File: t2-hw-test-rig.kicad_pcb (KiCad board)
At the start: 2 copper layers, 86.4 x 94 mm, 158 parts, among them J101 CONN_01X02, J102 BARREL_JACK, J103 CONN_01X02, J201 MICROUSB-TH, J202 CONN_01X02, J203 MICROUSB-TH, J204 USB_A_TH, J301 CONN_02x05, 0.05", Q101 pMOS, Q401 CJ2302, Q402 CJ2302, Q403 CJ2302, Q404 CJ2302, SW301 Switch_DPST, SW302 Switch_DPST, U101 MAX6102, U102 XC6206P332MR-G, U301 ATSAMD21J18A-MUT, U302 AAT4610, U303 AAT4610, U401 MAX9919FASA+, U402 MAX9919FASA+, U403 MAX9919FASA+, U404 MAX9919FASA+, U405 MAX9919FASA+, U501 TSV324IDT, U502 TSV324IDT, U503 TSV324IDT, X301 FC-135

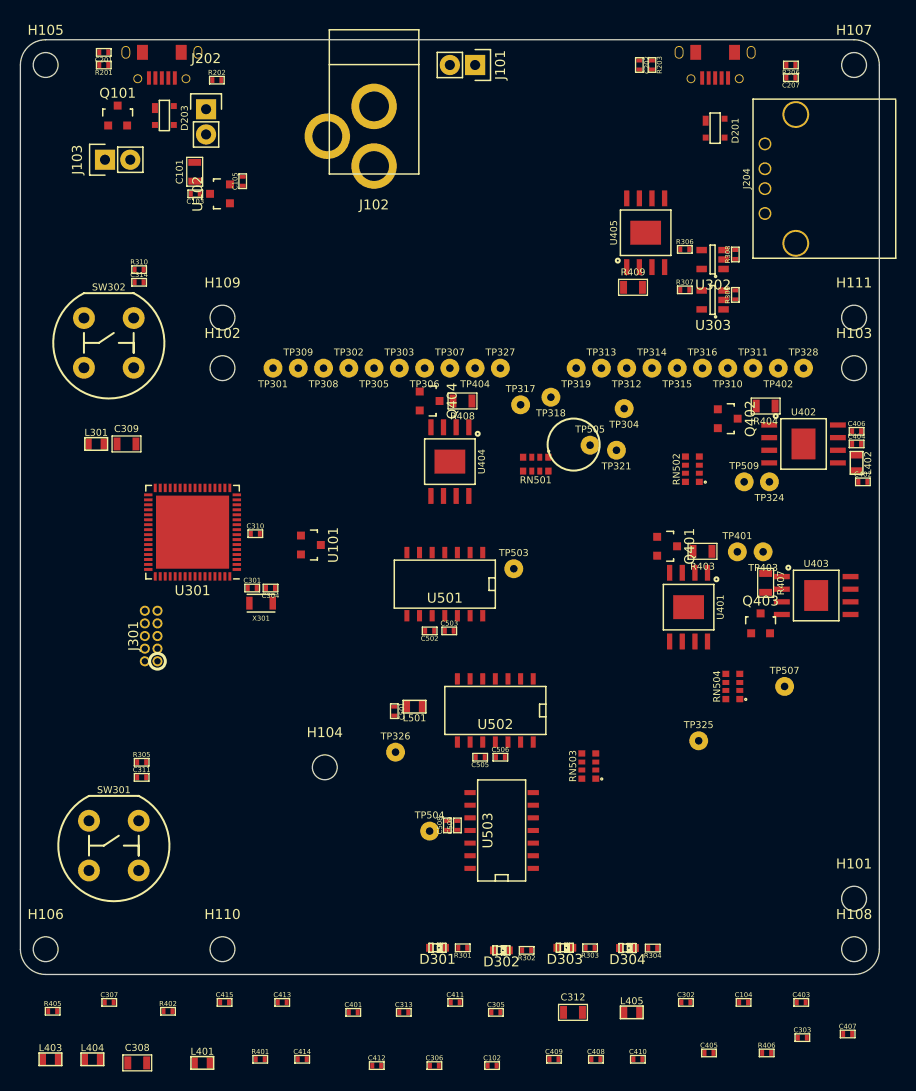
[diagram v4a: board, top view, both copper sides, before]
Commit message: moved mechanicals to a separate sheet
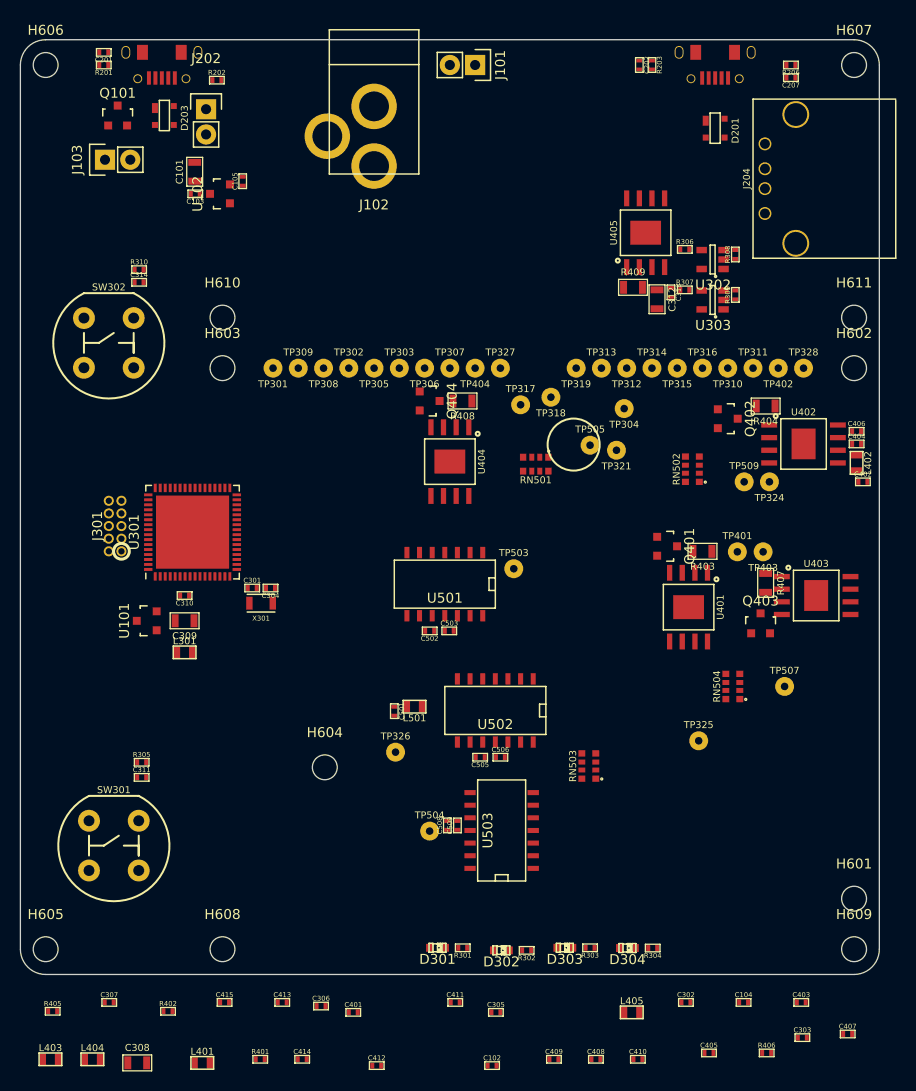
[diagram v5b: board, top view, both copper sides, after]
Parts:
- removed H101, H102, H103, H104, H105, H106, H107, H108, H109, H110, H111: M2.5, tm-kicad-lib:MountingHole_2-5mm
- added H601: M2.5, tm-kicad-lib:MountingHole_2-5mm, F.Cu at (134.6, 144.8)
- added H602: M2.5, tm-kicad-lib:MountingHole_2-5mm, F.Cu at (134.6, 91.4)
- added H603: M2.5, tm-kicad-lib:MountingHole_2-5mm, F.Cu at (71.1, 91.4)
- added H604: M2.5, tm-kicad-lib:MountingHole_2-5mm, F.Cu at (81.4, 131.6)
- added H605: M2.5, tm-kicad-lib:MountingHole_2-5mm, F.Cu at (53.3, 149.9)
- added H606: M2.5, tm-kicad-lib:MountingHole_2-5mm, F.Cu at (53.3, 61.0)
- added H607: M2.5, tm-kicad-lib:MountingHole_2-5mm, F.Cu at (134.6, 61.0)
- added H608: M2.5, tm-kicad-lib:MountingHole_2-5mm, F.Cu at (71.1, 149.9)
- added H609: M2.5, tm-kicad-lib:MountingHole_2-5mm, F.Cu at (134.6, 149.9)
- added H610: M2.5, tm-kicad-lib:MountingHole_2-5mm, F.Cu at (71.1, 86.4)
- added H611: M2.5, tm-kicad-lib:MountingHole_2-5mm, F.Cu at (134.6, 86.4)
- moved C313 77.2 mm to (116.2, 83.8), turned to 270 degrees
- moved C312 72.2 mm to (114.8, 84.5), turned to 270 degrees
- moved L301 22.8 mm to (67.3, 120.0)
- moved C309 18.7 mm to (67.3, 116.8), turned to 180 degrees
- moved U101 18.2 mm to (63.5, 116.8), turned to 90 degrees
- moved C306 12.9 mm to (81.0, 155.6)
- moved J301 11.6 mm to (60.3, 107.3)
- moved C310 9.44 mm to (67.3, 114.3), turned to 180 degrees
- turned U301 to 90 degrees

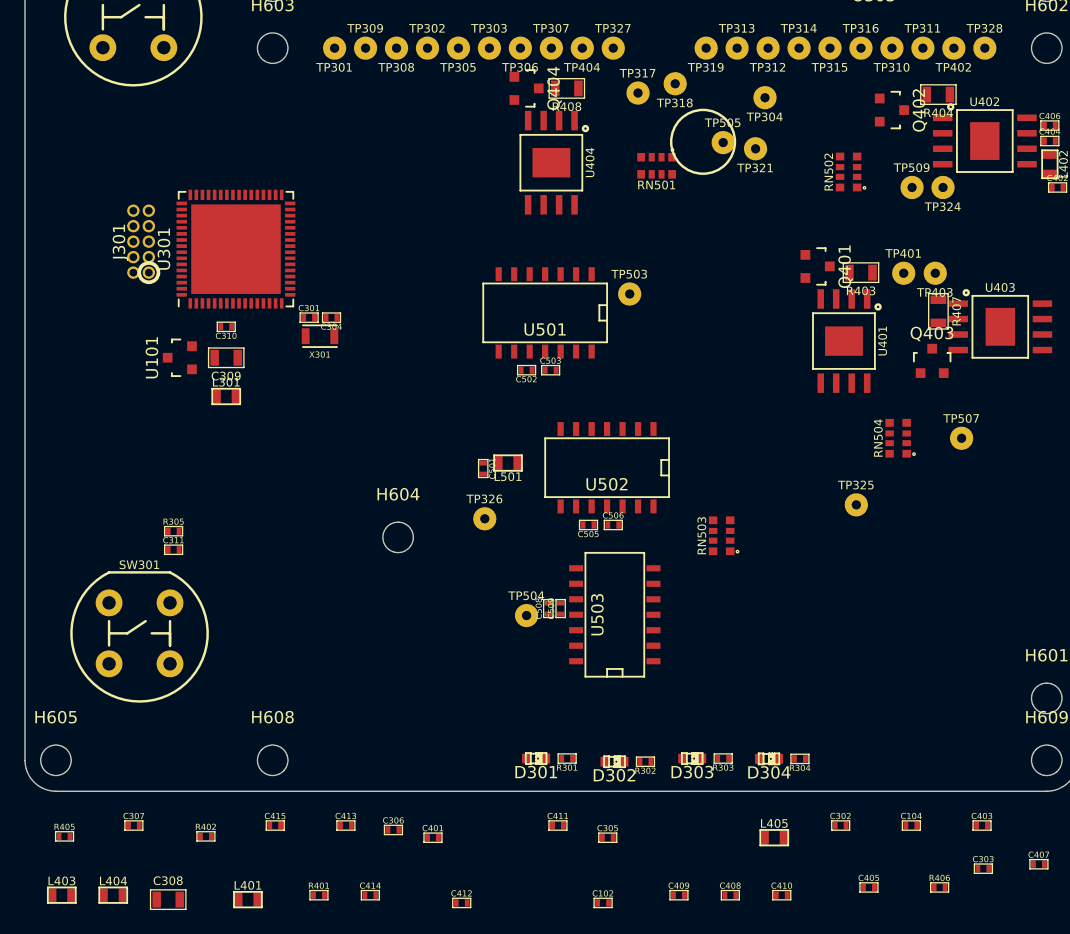
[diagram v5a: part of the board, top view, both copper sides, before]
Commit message: consolidated csa power, removed drill map text
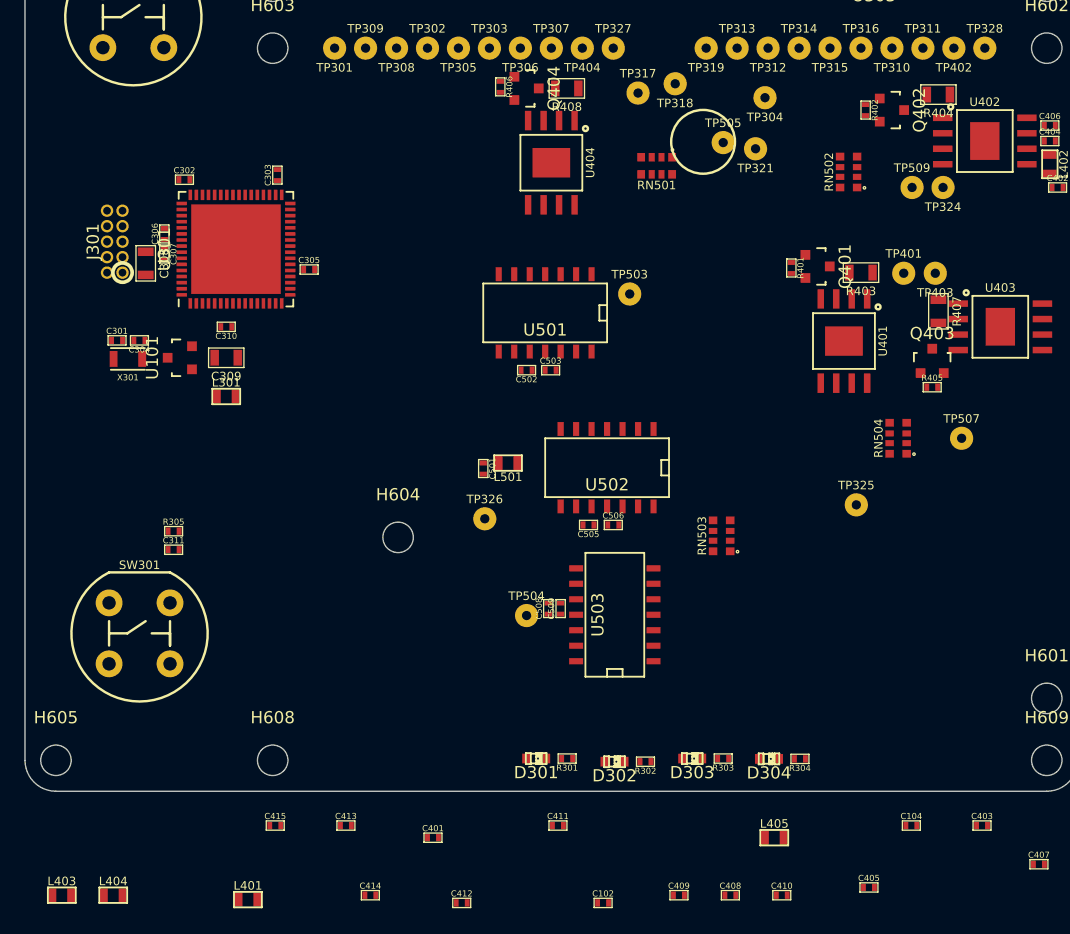
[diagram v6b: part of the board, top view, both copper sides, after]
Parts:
- moved C303 81.2 mm to (71.5, 101.9), turned to 90 degrees
- moved R402 80.5 mm to (119.8, 96.5), turned to 270 degrees
- moved R405 80.1 mm to (125.2, 119.3)
- moved C302 75.5 mm to (63.9, 102.2)
- moved R406 74.9 mm to (89.8, 94.6), turned to 270 degrees
- moved R401 64.4 mm to (113.7, 109.5), turned to 270 degrees
- moved C305 52.7 mm to (74.1, 109.6)
- moved C306 52.4 mm to (62.2, 106.7), turned to 90 degrees
- moved C308 52.2 mm to (60.7, 109.1), turned to 270 degrees
- moved C307 46.9 mm to (62.2, 108.3), turned to 270 degrees
- moved C301 15.9 mm to (58.4, 115.4)
- moved C304 15.9 mm to (60.2, 115.4)
- moved X301 15.9 mm to (59.2, 116.9)
- moved J301 2.16 mm to (58.2, 107.3)
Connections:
- C403 pad 1: /CURRENT/VCC_CSA_5VUSB0 -> /CURRENT/VCC_CSA
- C404 pad 1: /CURRENT/VCC_CSA_33PA -> /CURRENT/VCC_CSA
- C405 pad 1: /CURRENT/VCC_CSA_5VUSB0 -> /CURRENT/VCC_CSA
- C406 pad 1: /CURRENT/VCC_CSA_33PA -> /CURRENT/VCC_CSA
- C409 pad 1: /CURRENT/VCC_CSA_5VUSB1 -> /CURRENT/VCC_CSA
- C410 pad 1: /CURRENT/VCC_CSA_33PB -> /CURRENT/VCC_CSA
- C411 pad 1: /CURRENT/VCC_CSA_5VUSB1 -> /CURRENT/VCC_CSA
- C412 pad 1: /CURRENT/VCC_CSA_33PB -> /CURRENT/VCC_CSA
- C414 pad 1: /CURRENT/VCC_CSA_UUT -> /CURRENT/VCC_CSA
- C415 pad 1: /CURRENT/VCC_CSA_UUT -> /CURRENT/VCC_CSA
- L401 pad 1: /CURRENT/VCC_CSA_5VUSB0 -> /CURRENT/VCC_CSA
- U401 pad 8: /CURRENT/VCC_CSA_5VUSB0 -> /CURRENT/VCC_CSA
- U402 pad 8: /CURRENT/VCC_CSA_33PA -> /CURRENT/VCC_CSA
- U403 pad 8: /CURRENT/VCC_CSA_5VUSB1 -> /CURRENT/VCC_CSA
- U404 pad 8: /CURRENT/VCC_CSA_33PB -> /CURRENT/VCC_CSA
- U405 pad 8: /CURRENT/VCC_CSA_UUT -> /CURRENT/VCC_CSA

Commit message: placement "complete"
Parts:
- removed C402, C407, C408, C413: 100nF, tm-kicad-lib:SMD-0402-C
- removed L402, L403, L404, L405: 10uH, tm-kicad-lib:SMD-0603-R
- moved L401 101.7 mm to (118.1, 72.1), turned to 90 degrees
- moved C414 95.3 mm to (118.6, 74.2)
- moved C415 92.7 mm to (118.6, 75.4)
- moved C401 92.4 mm to (118.6, 70.4)
- moved C104 71.9 mm to (64.3, 114.6), turned to 180 degrees
- moved C411 59.6 mm to (133.9, 110.5), turned to 180 degrees
- moved C409 59.5 mm to (133.9, 109.2), turned to 180 degrees
- moved C410 58.9 mm to (98.3, 103.9), turned to 90 degrees
- moved C412 58.7 mm to (97.3, 103.9), turned to 90 degrees
- moved C102 54.5 mm to (64.0, 119.1), turned to 180 degrees
- moved C405 41.5 mm to (121.7, 118.9)
- moved C403 38.4 mm to (121.7, 117.6)
- moved J101 21.6 mm to (81.3, 76.2)
- moved C202 12.7 mm to (125.7, 60.2)
- moved R203 12.7 mm to (127.0, 60.2)
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
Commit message: drc tweaks
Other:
- net class Default: trace_width 0.2032 -> 0.254; via_dia 0.6 -> 0.635; via_drill 0.4 -> 0.4572
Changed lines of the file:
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@@
     (links 363)
     (no_connects 363)
-    (area 50.749999 58.369999 137.210001 152.450001)
+    (area 48.159999 55.4528 139.089201 155.040001)
     (thickness 1.6)
     (drawings 1404)
@@
   )
   (setup
-    (last_trace_width 0.2032)
+    (last_trace_width 0.254)
     (user_trace_width 0.2032)
     (user_trace_width 0.381)
@@
     (segment_width 0.2)
     (edge_width 0.1)
-    (via_size 0.6)
-    (via_drill 0.4)
+    (via_size 0.635)
+    (via_drill 0.4572)
     (via_min_size 0.4)
     (via_min_drill 0.3)
@@
   (net_class Default "This is the default net class."
     (clearance 0.2032)
-    (trace_width 0.2032)
-    (via_dia 0.6)
-    (via_drill 0.4)
+    (trace_width 0.254)
+    (via_dia 0.635)
+    (via_drill 0.4572)
     (uvia_dia 0.3)
     (uvia_drill 0.1)
